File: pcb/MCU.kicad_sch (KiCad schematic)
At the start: 0 parts

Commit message: pcb: mcu schematic start
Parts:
- added C39, C40, C42: 100nF, symbol Device:C
- added C41: 4.7uF, symbol Device:C
- added STM32UF9NJH6Q_CUSTOM1: (no value), TFBGA216_13X13_STM, symbol STM32U5F0NJH6Q_custom:STM32U5F9NJH6Q_CUSTOM
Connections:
- new net: C40.1, C41.1, C42.1, STM32UF9NJH6Q_CUSTOM1.E8 (VDDIO2), STM32UF9NJH6Q_CUSTOM1.G11 (VDDIO2)
- new net GND: C39.2, C40.2, C41.2, C42.2
- new net VDDUSB: C39.1, STM32UF9NJH6Q_CUSTOM1.E9 (VDDUSB)
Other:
- title: (none) -> MCU design

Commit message: pcb: mcu schematic start pt 2
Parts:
- added C43, C44: 6.8pF, symbol Device:C
- added Y2: 16MHz, symbol Device:Crystal_GND24_Small
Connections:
- net at STM32UF9NJH6Q_CUSTOM1.N1 (PH0-OSC_IN): now also C43.2, Y2.1
- net at STM32UF9NJH6Q_CUSTOM1.N2 (PH1-OSC_OUT): now also C44.2
- new net: Y2.2 (G), Y2.4 (G)

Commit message: pcb: created the MCU design from the slides
In case we end up using this I believe it is nice to have it available just in case
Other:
- added sheet STM32U535CE (STM32U535CE.kicad_sch)
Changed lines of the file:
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@@
+		)
+	)
+	(sheet
+		(at 20.32 30.48)
+		(size 24.13 13.97)
+		(exclude_from_sim no)
+		(in_bom yes)
+		(on_board yes)
+		(dnp no)
+		(fields_autoplaced yes)
+		(stroke
+			(width 0.1524)
+			(type solid)
+		)
+		(fill
+			(color 0 0 0 0)
+		)
+		(property "Sheetname" "STM32U535CE"
+			(at 20.32 29.7684 0)
+			(show_name no)
+			(do_not_autoplace no)
+			(effects
+				(font
+					(size 1.27 1.27)
+				)
+				(justify left bottom)
+			)
+		)
+		(property "Sheetfile" "STM32U535CE.kicad_sch"
+			(at 20.32 45.0346 0)
+			(show_name no)
+			(do_not_autoplace no)
+			(effects
+				(font
+					(size 1.27 1.27)
+				)
+				(justify left top)
+			)
+		)
+		(instances
+			(project "tdt4295"
+				(path "/603dd496-f9c4-4a31-9104-19eec41ebc98/59405b24-6536-4799-b908-ee0def989f5c"
+					(page "6")
+				)
+			)
 		)
 	)

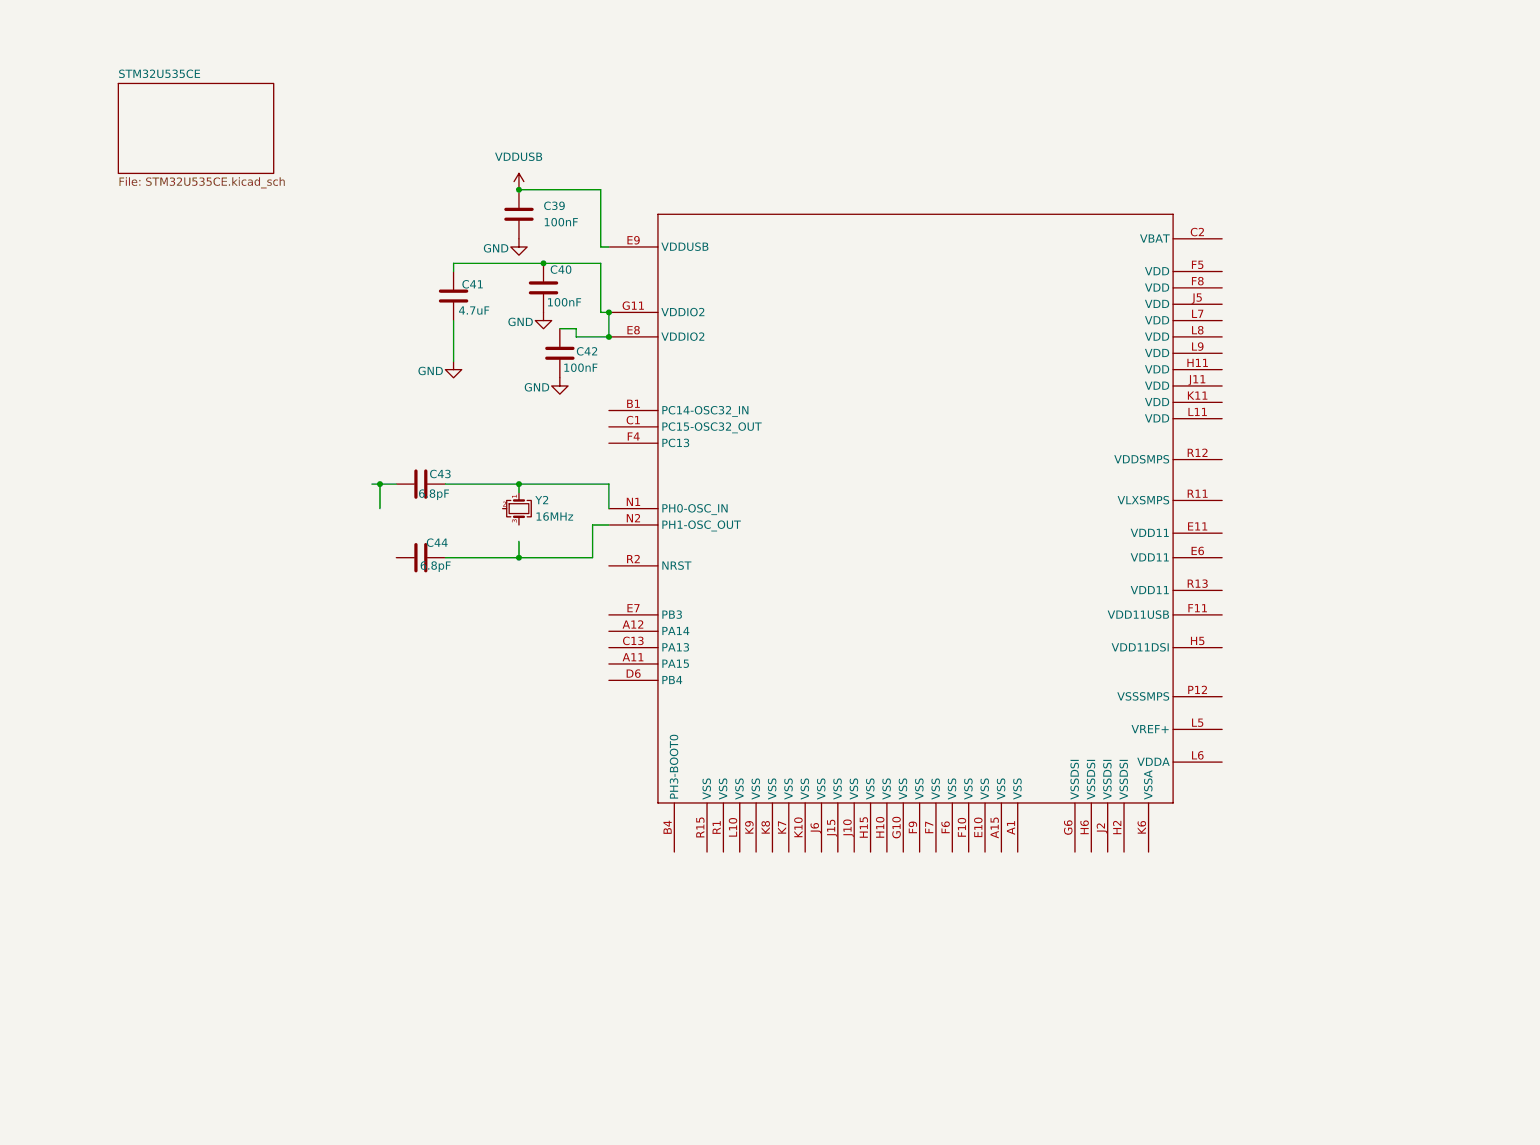
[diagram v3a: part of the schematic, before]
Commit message: pcb: mcu schematic almost finished2
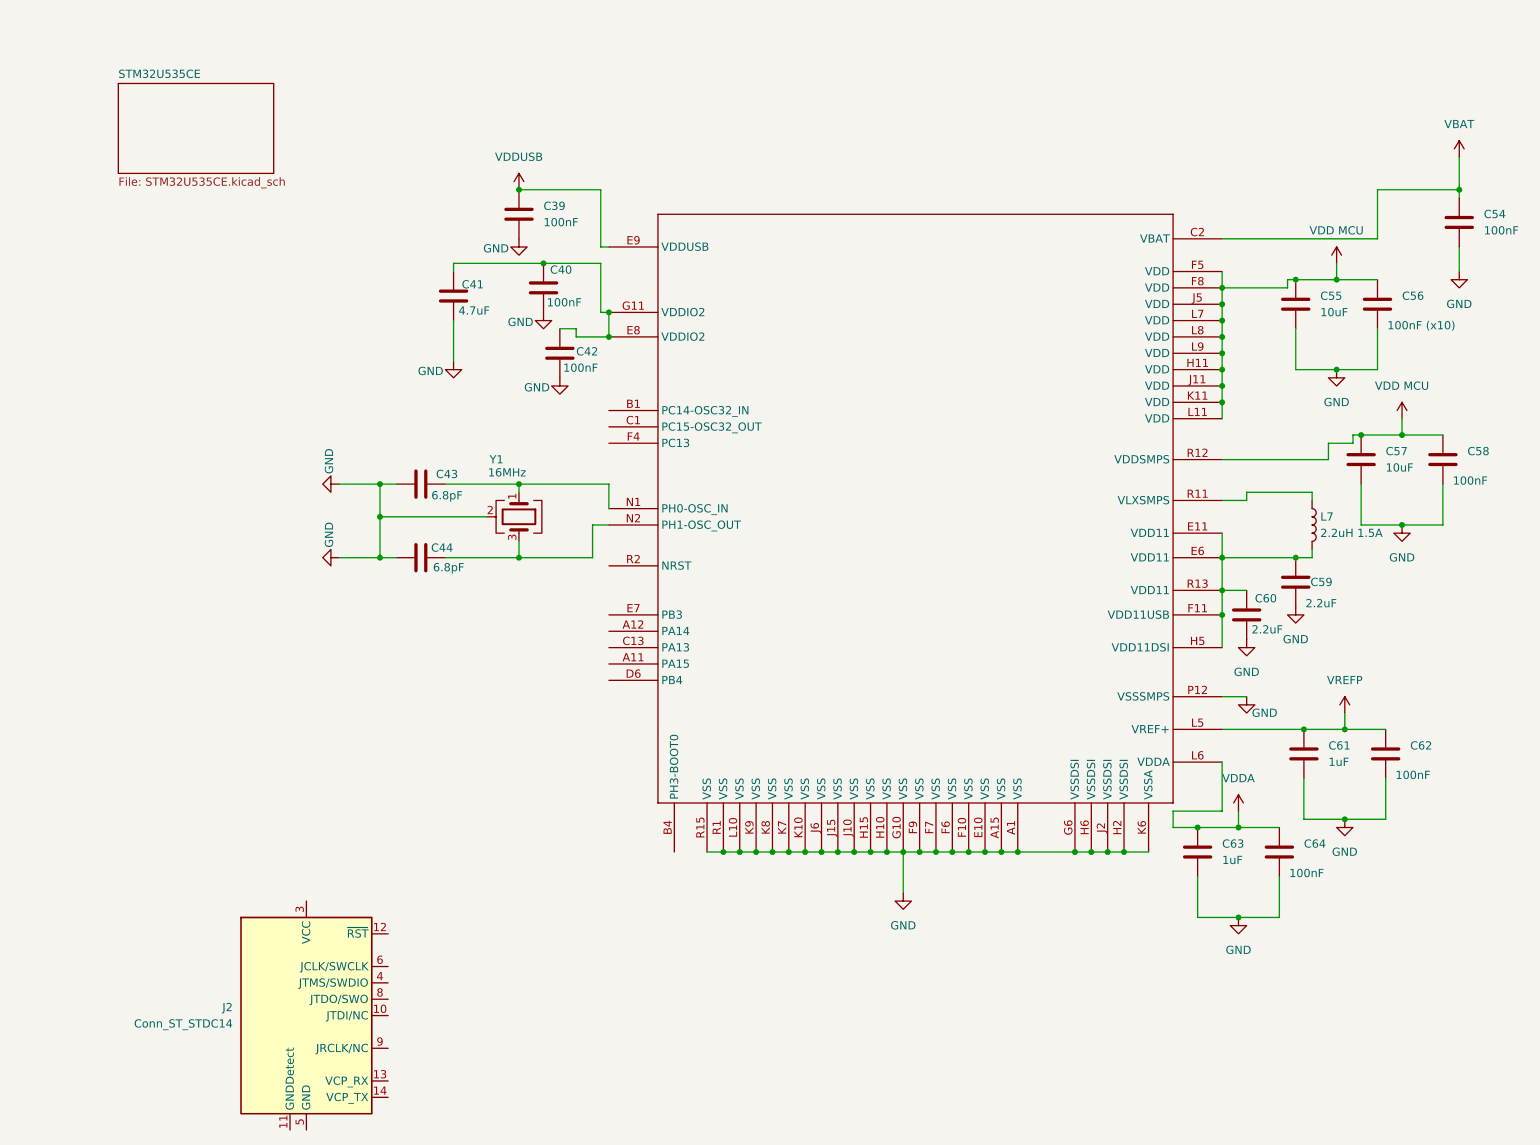
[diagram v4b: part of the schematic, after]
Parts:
- removed Y2: 16MHz, symbol Device:Crystal_GND24_Small
- added C54, C58, C62, C64: 100nF, symbol Device:C
- added C55, C57: 10uF, symbol Device:C
- added C56: 100nF (x10), symbol Device:C
- added C59, C60: 2.2uF, symbol Device:C
- added C61, C63: 1uF, symbol Device:C
- added J2: Conn_ST_STDC14, Package_LCC:PLCC-84_29.3x29.3mm_P1.27mm, symbol Connector:Conn_ST_STDC14
- added L7: 2.2uH 1.5A, Package_SON:WSON-8-1EP_6x5mm_P1.27mm_EP3.4x4mm, symbol Device:L
- added Y1: 16MHz, Oscillator:Oscillator_SMD_Fordahl_DFAS11-4Pin_7.0x5.0mm, symbol Device:Crystal_GND24
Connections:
- net GND: now also C43.1, C44.1, STM32UF9NJH6Q_CUSTOM1.A1 (VSS), STM32UF9NJH6Q_CUSTOM1.A15 (VSS), STM32UF9NJH6Q_CUSTOM1.E10 (VSS), STM32UF9NJH6Q_CUSTOM1.F10 (VSS), STM32UF9NJH6Q_CUSTOM1.F6 (VSS), STM32UF9NJH6Q_CUSTOM1.F7 (VSS), STM32UF9NJH6Q_CUSTOM1.F9 (VSS), STM32UF9NJH6Q_CUSTOM1.G10 (VSS), STM32UF9NJH6Q_CUSTOM1.G6 (VSSDSI), STM32UF9NJH6Q_CUSTOM1.H10 (VSS), STM32UF9NJH6Q_CUSTOM1.H15 (VSS), STM32UF9NJH6Q_CUSTOM1.H2 (VSSDSI), STM32UF9NJH6Q_CUSTOM1.H6 (VSSDSI), STM32UF9NJH6Q_CUSTOM1.J10 (VSS), STM32UF9NJH6Q_CUSTOM1.J15 (VSS), STM32UF9NJH6Q_CUSTOM1.J2 (VSSDSI), STM32UF9NJH6Q_CUSTOM1.J6 (VSS), STM32UF9NJH6Q_CUSTOM1.K10 (VSS), STM32UF9NJH6Q_CUSTOM1.K6 (VSSA), STM32UF9NJH6Q_CUSTOM1.K7 (VSS), STM32UF9NJH6Q_CUSTOM1.K8 (VSS), STM32UF9NJH6Q_CUSTOM1.K9 (VSS), STM32UF9NJH6Q_CUSTOM1.L10 (VSS), STM32UF9NJH6Q_CUSTOM1.P12 (VSSSMPS), STM32UF9NJH6Q_CUSTOM1.R1 (VSS), STM32UF9NJH6Q_CUSTOM1.R15 (VSS), C54.2, C55.2, C56.2, C57.2, C58.2, C59.2, C60.2, C61.2, C62.2, C63.2, C64.2, Y1.2 (G), Y1.4 (G)
- net at C43.2, STM32UF9NJH6Q_CUSTOM1.N1 (PH0-OSC_IN): now also Y1.1
- net at C44.2, STM32UF9NJH6Q_CUSTOM1.N2 (PH1-OSC_OUT): now also Y1.3
- net VBAT: now reaches STM32UF9NJH6Q_CUSTOM1.C2 (VBAT)
- net VBAT: now also C54.1
- net at STM32UF9NJH6Q_CUSTOM1.E11 (VDD11): now also STM32UF9NJH6Q_CUSTOM1.E6 (VDD11), STM32UF9NJH6Q_CUSTOM1.F11 (VDD11USB), STM32UF9NJH6Q_CUSTOM1.H5 (VDD11DSI), STM32UF9NJH6Q_CUSTOM1.R13 (VDD11), C59.1, C60.1, L7.2
- net VDD MCU: now reaches STM32UF9NJH6Q_CUSTOM1.F5 (VDD)
- net VDD MCU: now also STM32UF9NJH6Q_CUSTOM1.F8 (VDD), STM32UF9NJH6Q_CUSTOM1.H11 (VDD), STM32UF9NJH6Q_CUSTOM1.J11 (VDD), STM32UF9NJH6Q_CUSTOM1.J5 (VDD), STM32UF9NJH6Q_CUSTOM1.K11 (VDD), STM32UF9NJH6Q_CUSTOM1.L11 (VDD), STM32UF9NJH6Q_CUSTOM1.L7 (VDD), STM32UF9NJH6Q_CUSTOM1.L8 (VDD), STM32UF9NJH6Q_CUSTOM1.L9 (VDD), STM32UF9NJH6Q_CUSTOM1.R12 (VDDSMPS), C55.1, C56.1, C57.1, C58.1
- net VREFP: now reaches STM32UF9NJH6Q_CUSTOM1.L5 (VREF+)
- net VREFP: now also C61.1, C62.1
- net VDDA: now reaches STM32UF9NJH6Q_CUSTOM1.L6 (VDDA)
- net VDDA: now also C63.1, C64.1
- net at STM32UF9NJH6Q_CUSTOM1.R11 (VLXSMPS): now also L7.1
- new net: J2.5 (GND), J2.7 (GND)

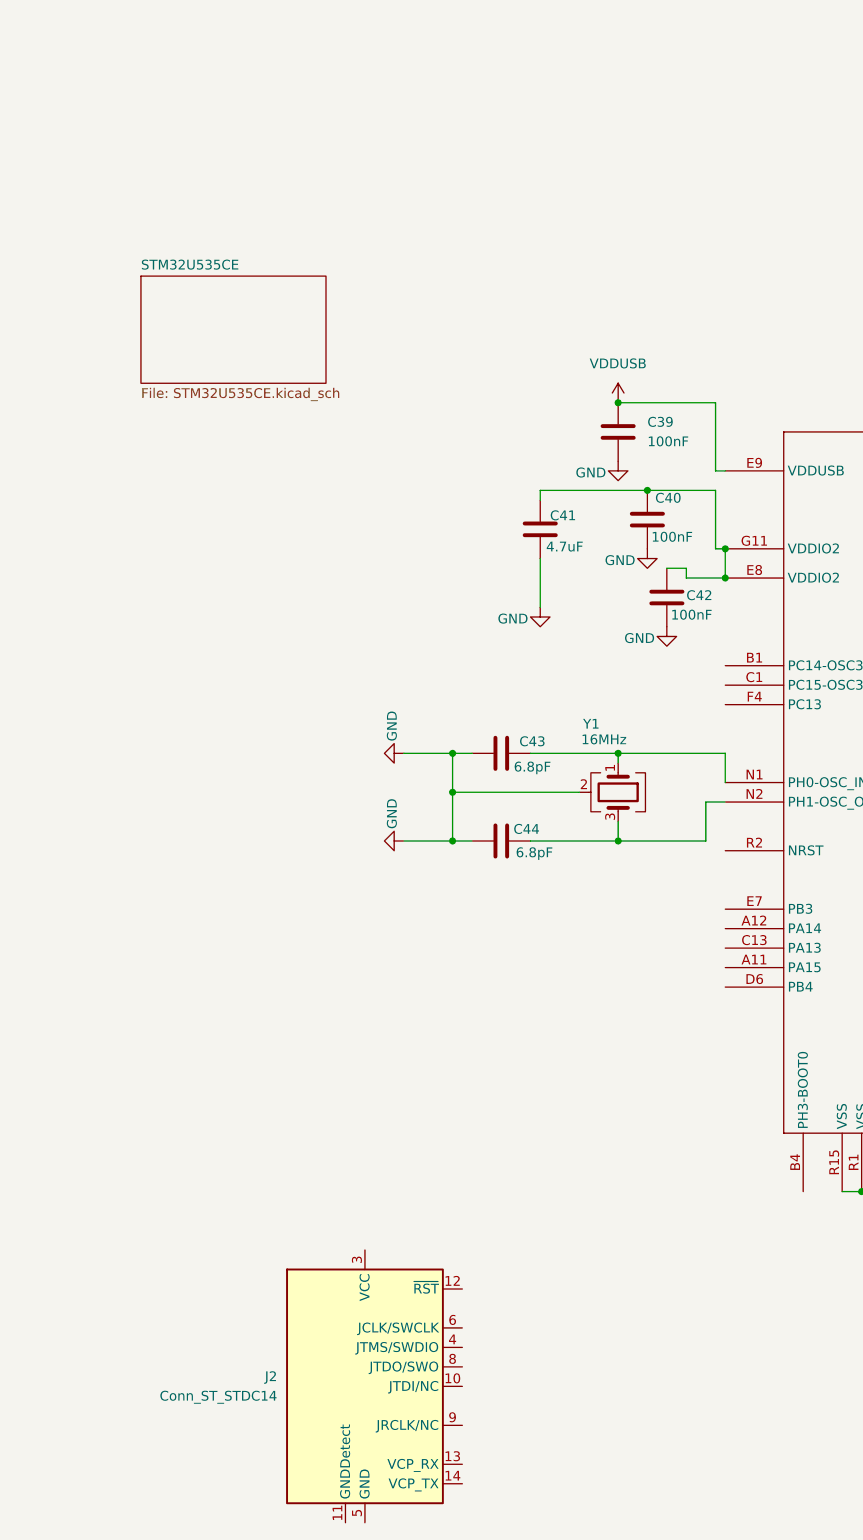
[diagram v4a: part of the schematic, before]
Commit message: started new MCU design impl
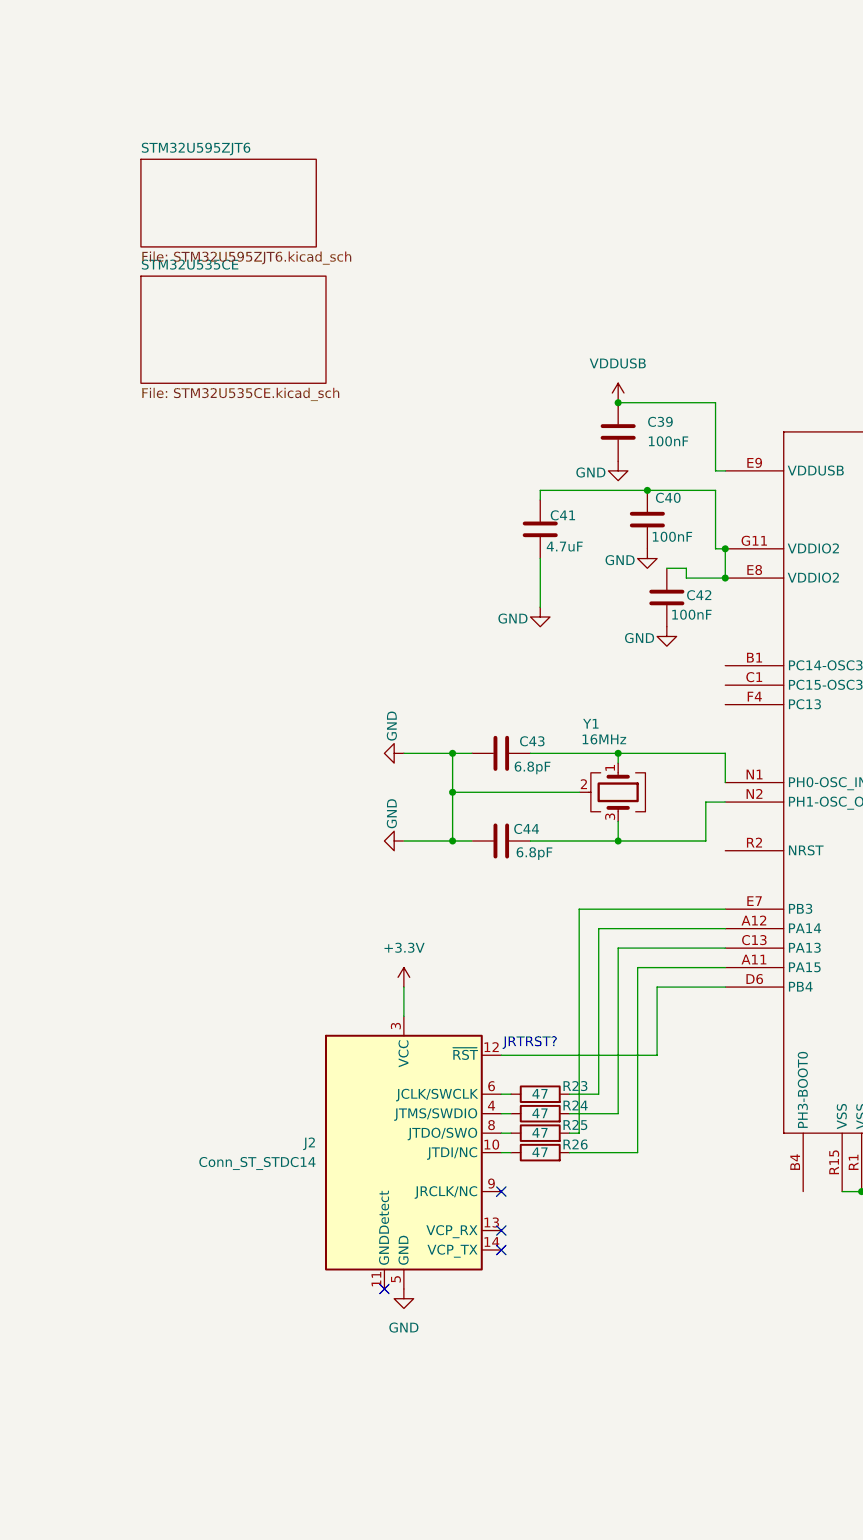
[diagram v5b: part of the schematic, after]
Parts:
- added R23, R24, R25, R26: 47, symbol Device:R
- J2: footprint Package_LCC:PLCC-84_29.3x29.3mm_P1.27mm -> (none)
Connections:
- net GND: now also J2.5 (GND), J2.7 (GND)
- net at J2.10 (JTDI/NC): now also R26.1
- net at J2.12 (~{RST}): now also STM32UF9NJH6Q_CUSTOM1.D6 (PB4)
- net +3.3V: now reaches J2.3 (VCC)
- net at J2.4 (JTMS/SWDIO): now also R24.1
- net at J2.6 (JCLK/SWCLK): now also R23.1
- net at J2.8 (JTDO/SWO): now also R25.1
- net at STM32UF9NJH6Q_CUSTOM1.A11 (PA15): now also R26.2
- net at STM32UF9NJH6Q_CUSTOM1.A12 (PA14): now also R23.2
- net at STM32UF9NJH6Q_CUSTOM1.C13 (PA13): now also R24.2
- net at STM32UF9NJH6Q_CUSTOM1.E7 (PB3): now also R25.2
- no-connect marks 0 -> 4
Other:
- added sheet STM32U595ZJT6 (STM32U595ZJT6.kicad_sch)
- note added: "JRTRST?"

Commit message: started usb_c imp
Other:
- added sheet usb_c (usb_c.kicad_sch)
- moved on the sheet: C39, C40, C41, C42, C43, C44, C54, C55, C56, C57, C58, C59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

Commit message: pcb: changes usbc and add input power
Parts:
- added C103: 10uF, symbol Device:C
- added C104, C105, C106, C107, C108, C109, C110, C111, C112, C115, C116, C83: 100nF, symbol Device:C
- added C113, C114: 6.8pF, symbol Device:C
- added C117, C118, C120: 1uF, symbol Device:C
- added C119: 4.7uF, symbol Device:C
- added J6: Conn_ST_STDC14, symbol Connector:Conn_ST_STDC14
- added R35, R36, R37, R38: 47, symbol Device:R
- added U10: STM32U595ZJTx, Package_QFP:LQFP-144_20x20mm_P0.5mm, symbol MCU_ST_STM32U5:STM32U595ZJTx
- added Y5: 16MHz, Oscillator:Oscillator_SMD_Fordahl_DFAS11-4Pin_7.0x5.0mm, symbol Device:Crystal_GND24
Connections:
- net +3.3V: now also C103.1, C104.1, C105.1, C106.1, C107.1, C108.1, C109.1, C110.1, C111.1, C112.1, J6.3 (VCC), U10.108 (VDD), U10.121 (VDD), U10.144 (VDD), U10.17 (VDD), U10.39 (VDD), U10.52 (VDD), U10.62 (VDD), U10.72 (VDD), U10.84 (VDD)
- net GND: now also C103.2, C104.2, C105.2, C106.2, C107.2, C108.2, C109.2, C110.2, C111.2, C112.2, C113.1, C114.1, C115.2, C116.2, C117.2, C118.2, C119.2, C120.2, C83.2, J6.5 (GND), J6.7 (GND), U10.107 (VSS), U10.120 (VSS), U10.130 (VSS), U10.143 (VSS), U10.16 (VSS), U10.30 (VSSA), U10.31 (VREF-), U10.38 (VSS), U10.51 (VSS), U10.61 (VSS), U10.71 (VSS), U10.83 (VSS), U10.94 (VSS), Y5.2 (G), Y5.4 (G)
- net VBAT: now also C120.1, U10.6 (VBAT)
- net VDDA: now also C115.1, C117.1, U10.33 (VDDA)
- net VDDUSB: now also C83.1, U10.106 (VDDUSB)
- net VREFP: now also C116.1, C118.1, U10.32 (VREF+)
- new net: R37.1, U10.133 (PB3)
- new net: J6.8 (JTDO/SWO), R37.2
- new net: R35.1, U10.109 (PA14)
- new net: J6.6 (JCLK/SWCLK), R35.2
- new net: R38.1, U10.110 (PA15)
- new net: J6.10 (JTDI/NC), R38.2
- new net: C113.2, U10.23 (PH0), Y5.1
- new net: C114.2, U10.24 (PH1), Y5.3
- new net: C119.1, U10.70 (VCAP)
- new net: J6.12 (~{RST}), U10.25 (NRST)
- new net: J6.4 (JTMS/SWDIO), R36.2
- new net: R36.1, U10.105 (PA13)
- new net USB_FS_N: U10.103 (PA11)
- new net USB_FS_P: U10.104 (PA12)
- no-connect marks 4 -> 8
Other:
- removed sheet STM32U595ZJT6
- moved on the sheet: C39, C40, C41, C42, C43, C44, C54, C55, C56, C57, C58, C59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
